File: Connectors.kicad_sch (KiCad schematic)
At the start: 6 parts, among them J2 USB_C_Receptacle_USB2.0_16P, J5 Conn_01x02_Socket, J6 Conn_01x02_Socket, U3 USBLC6-2SC6

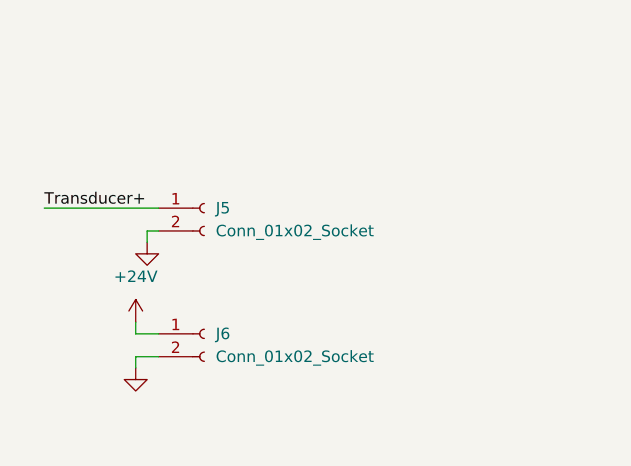
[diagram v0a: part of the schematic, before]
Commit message: Updated connectors to molex 2 pin
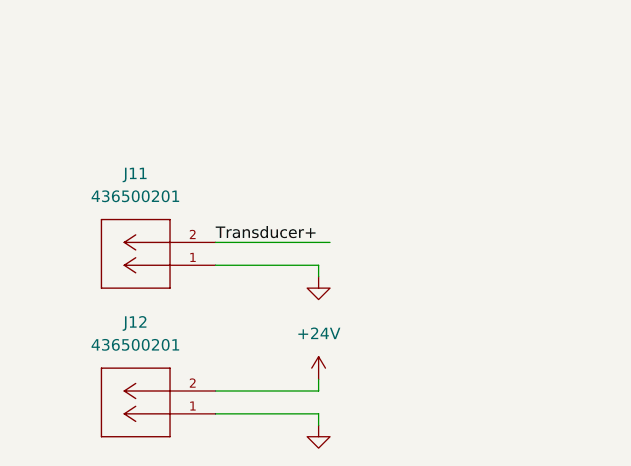
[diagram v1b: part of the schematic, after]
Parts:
- removed J5, J6: Conn_01x02_Socket, symbol Connector:Conn_01x02_Socket
- added J11, J12: 436500201, 436500201:CONN_SD-43650-001_02_MOL, symbol 436500201:436500201
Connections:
- net +24V: now also J12.2
- net GND: now also J11.1, J12.1
- net Transducer+: now also J11.2

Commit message: Added changes to pass ERC check
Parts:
- renumbered J2 to J1, J11 to J2, J12 to J3, R3 to R13, R4 to R14, U3 to U5
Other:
- moved on the sheet: J2, J3

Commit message: added footprints to every component except inductors. That will be in the next commit
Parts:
- J1: footprint (none) -> Connector_USB:USB_C_Receptacle_GCT_USB4105-xx-A_16P_TopMnt_Horizontal
- R13, R14: footprint (none) -> Resistor_SMD:R_0402_1005Metric
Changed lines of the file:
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@@
 			)
 		)
-		(property "Footprint" ""
+		(property "Footprint" "Connector_USB:USB_C_Receptacle_GCT_USB4105-xx-A_16P_TopMnt_Horizontal"
 			(at 53.34 54.61 0)
 			(hide yes)
@@
 			)
 		)
-		(property "Footprint" ""
+		(property "Footprint" "Resistor_SMD:R_0402_1005Metric"
 			(at 74.422 66.04 90)
 			(hide yes)
@@
 			)
 		)
-		(property "Footprint" ""
+		(property "Footprint" "Resistor_SMD:R_0402_1005Metric"
 			(at 74.168 66.04 90)
 			(hide yes)

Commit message: Adding some DRC constraints. Must finish adding stackup and predefined sizes
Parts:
- added J10: 436500201, 436500201:CONN_SD-43650-001_02_MOL, symbol 436500201:436500201
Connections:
- net +5V: now also J10.2
- net GND: now also J10.1
